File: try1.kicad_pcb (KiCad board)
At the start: 2 copper layers, 168.9 x 102 mm, 33 parts, among them J10 Archon-connector-modules-Driv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, J11 Archon-connector-modules-Driv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, J2 Archon-connector-modules-Heat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, J21 DB37, J22 DB37, J3 Archon-connector-modules-Driv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, J31 DB9, J4 Archon-connector-modules-LVBi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, J41 CONN_DVI, J5 Archon-connector-modules-ADC, J6 Archon-connector-modules-ADC, J7 Archon-connector-modules-ADC, J8 Archon-connector-modules-ADC, J9 Archon-connector-modules-HVBi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, P1 CONN_02X02

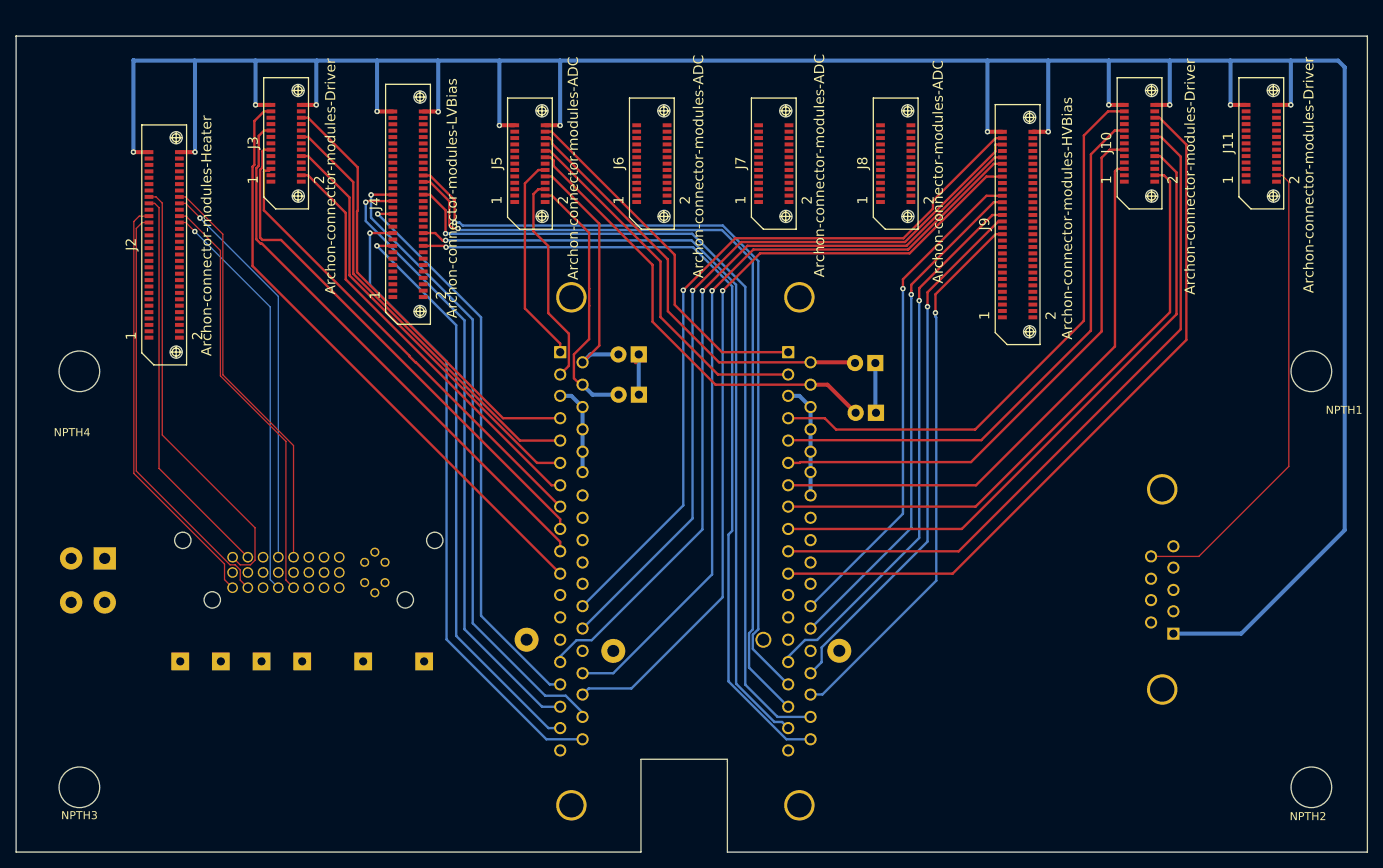
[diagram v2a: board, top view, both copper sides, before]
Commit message: WIP Add Last Driver Traces
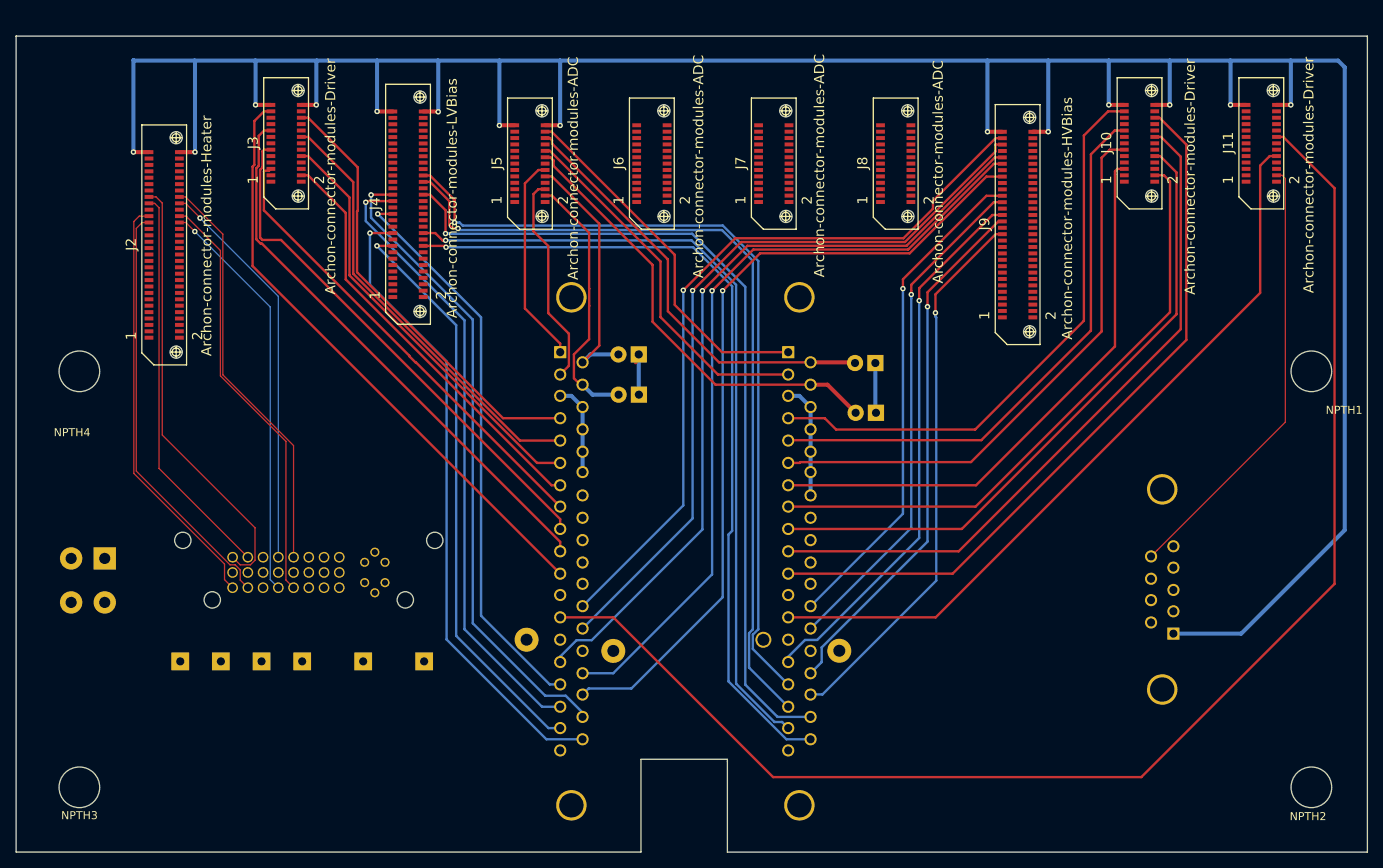
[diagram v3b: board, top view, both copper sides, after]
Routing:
- net /~ResetLog_L: track 0.41 -> 174.9 mm
- net /~ResetLog_R: track 0.00 -> 94.2 mm
- net FLASH_V: track 59.3 -> 55.5 mm
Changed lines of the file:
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@@
     (thickness 1.6)
     (drawings 37)
-    (tracks 527)
+    (tracks 539)
     (zones 0)
     (modules 33)
@@
   (segment (start 192.37 36.66) (end 192.37 61.08) (width 0.3) (layer F.Cu) (net 319))
   (segment (start 189.01214 33.30214) (end 192.37 36.66) (width 0.3) (layer F.Cu) (net 319))
+  (segment (start 203.63992 38.09766) (end 202.79001 38.09766) (width 0.3) (layer F.Cu) (net 320))
+  (segment (start 161.042 95.755) (end 142.603 95.755) (width 0.3) (layer F.Cu) (net 320))
+  (segment (start 202.79001 38.09766) (end 201.5982 39.28947) (width 0.3) (layer F.Cu) (net 320))
+  (segment (start 201.5982 39.28947) (end 201.5982 55.1988) (width 0.3) (layer F.Cu) (net 320))
+  (segment (start 201.5982 55.1988) (end 161.042 95.755) (width 0.3) (layer F.Cu) (net 320))
+  (segment (start 203.63992 35.70244) (end 204.48983 35.70244) (width 0.3) (layer F.Cu) (net 321))
+  (segment (start 140.7144 115.727) (end 120.7424 95.755) (width 0.3) (layer F.Cu) (net 321))
+  (segment (start 120.7424 95.755) (end 114.103 95.755) (width 0.3) (layer F.Cu) (net 321))
+  (segment (start 204.48983 35.70244) (end 210.8946 42.10721) (width 0.3) (layer F.Cu) (net 321))
+  (segment (start 210.8946 42.10721) (end 210.8946 91.5716) (width 0.3) (layer F.Cu) (net 321))
+  (segment (start 210.8946 91.5716) (end 186.7392 115.727) (width 0.3) (layer F.Cu) (net 321))
+  (segment (start 186.7392 115.727) (end 140.7144 115.727) (width 0.3) (layer F.Cu) (net 321))
   (segment (start 203.63992 35.70244) (end 204.050132 35.70244) (width 0.1524) (layer F.Cu) (net 321) (status 30))
-  (segment (start 203.63992 40.49796) (end 204.34223 40.49796) (width 0.1524) (layer F.Cu) (net 322) (status 10))
-  (segment (start 204.34223 40.49796) (end 205.1812 41.33693) (width 0.1524) (layer F.Cu) (net 322))
-  (segment (start 205.1812 41.33693) (end 205.1812 76.8858) (width 0.1524) (layer F.Cu) (net 322))
-  (segment (start 205.1812 76.8858) (end 193.929 88.138) (width 0.1524) (layer F.Cu) (net 322))
-  (segment (start 193.929 88.138) (end 187.96 88.138) (width 0.1524) (layer F.Cu) (net 322) (status 20))
+  (segment (start 188.721999 87.376001) (end 187.96 88.138) (width 0.1524) (layer F.Cu) (net 322))
+  (segment (start 204.743788 71.354212) (end 188.721999 87.376001) (width 0.1524) (layer F.Cu) (net 322))
+  (segment (start 204.743788 40.899518) (end 204.743788 71.354212) (width 0.1524) (layer F.Cu) (net 322))
+  (segment (start 204.34223 40.49796) (end 204.743788 40.899518) (width 0.1524) (layer F.Cu) (net 322))
+  (segment (start 203.63992 40.49796) (end 204.34223 40.49796) (width 0.1524) (layer F.Cu) (net 322))
   (segment (start 135.6 54.369388) (end 130.722228 49.491616) (width 0.3) (layer B.Cu) (net 343))
   (segment (start 130.722228 49.491616) (end 99.829114 49.491616) (width 0.3) (layer B.Cu) (net 343))

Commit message: Finish Main Rerouting After Edge, High Current Fixes
This is a milestone.  After updating the size/edge of the board
and correcting the erroneous connections that were supposed to be
high current biases, I have *roughly* placed most of the traces.
I still need to finish the Heater traces and adjust all of the traces
for ideal spacing.

First, however, I'm going to expose GPIO pins; then I'll make the final
passes on the routes.
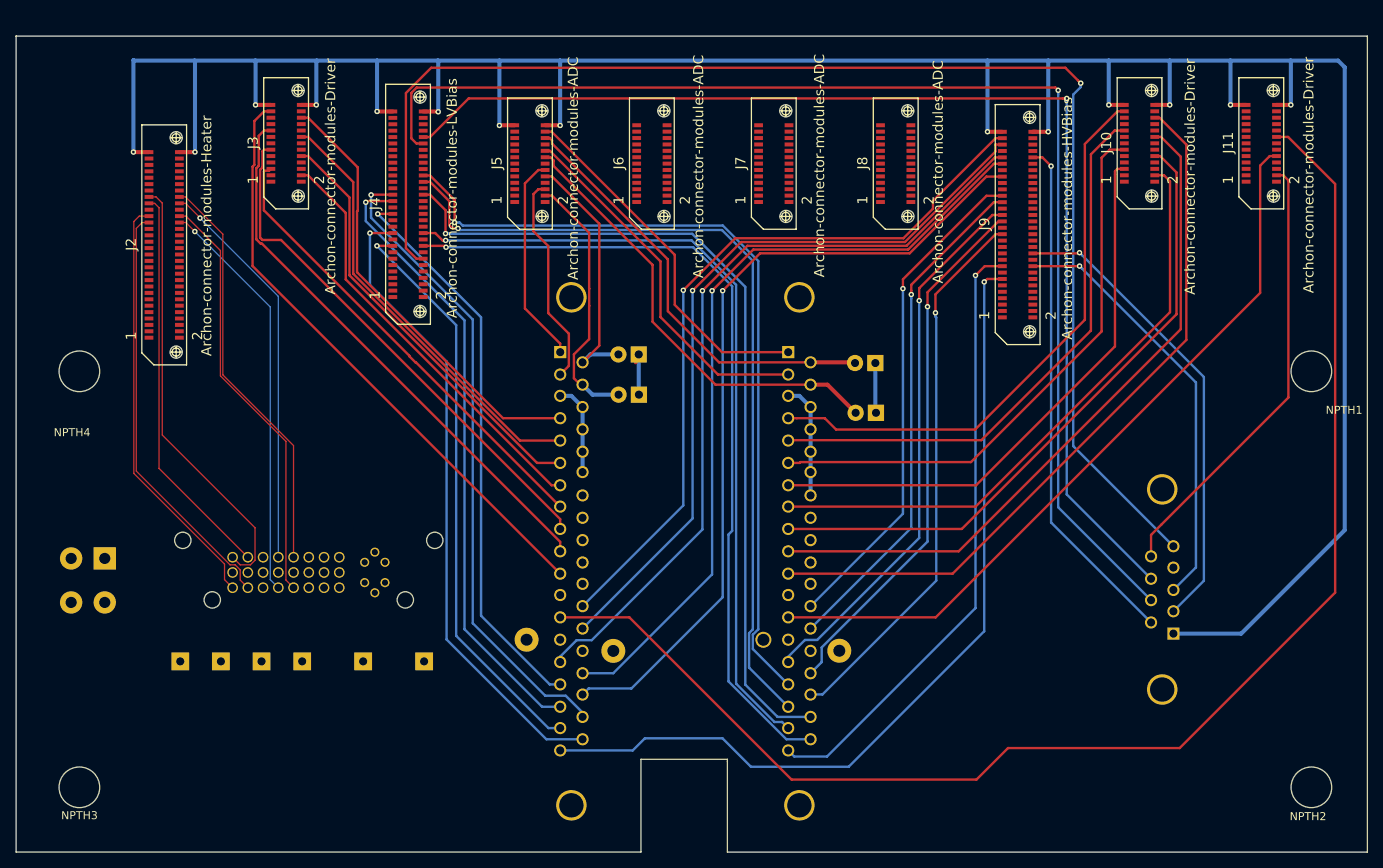
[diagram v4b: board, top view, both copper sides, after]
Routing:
- net LED_+15V: track 0.00 -> 172.0 mm, vias 0 -> 1
- net SEL_LED_1: track 0.00 -> 157.2 mm, vias 0 -> 1
- net SEL_LED_2: track 0.00 -> 146.8 mm, vias 0 -> 1
- net /+5V_L: track 0.00 -> 108.2 mm, vias 0 -> 1
- net /+5V_R: track 0.00 -> 76.8 mm, vias 0 -> 1
- net SHUT_OUT: track 0.00 -> 65.0 mm, vias 0 -> 1
- net LED_PWR: track 0.00 -> 58.7 mm, vias 0 -> 1
- net LED_+5: track 0.00 -> 53.5 mm, vias 0 -> 1
- net /~ResetLog_L: track 174.9 -> 176.2 mm
- net /S3X: track 72.6 -> 72.0 mm

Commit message: Expose GPIO Pins
I'm not sure this is exactly what we want, but the core is done.  If we
want to change the footprint for these pins or move them, it will be
relatively easy, now that the connections have been made.
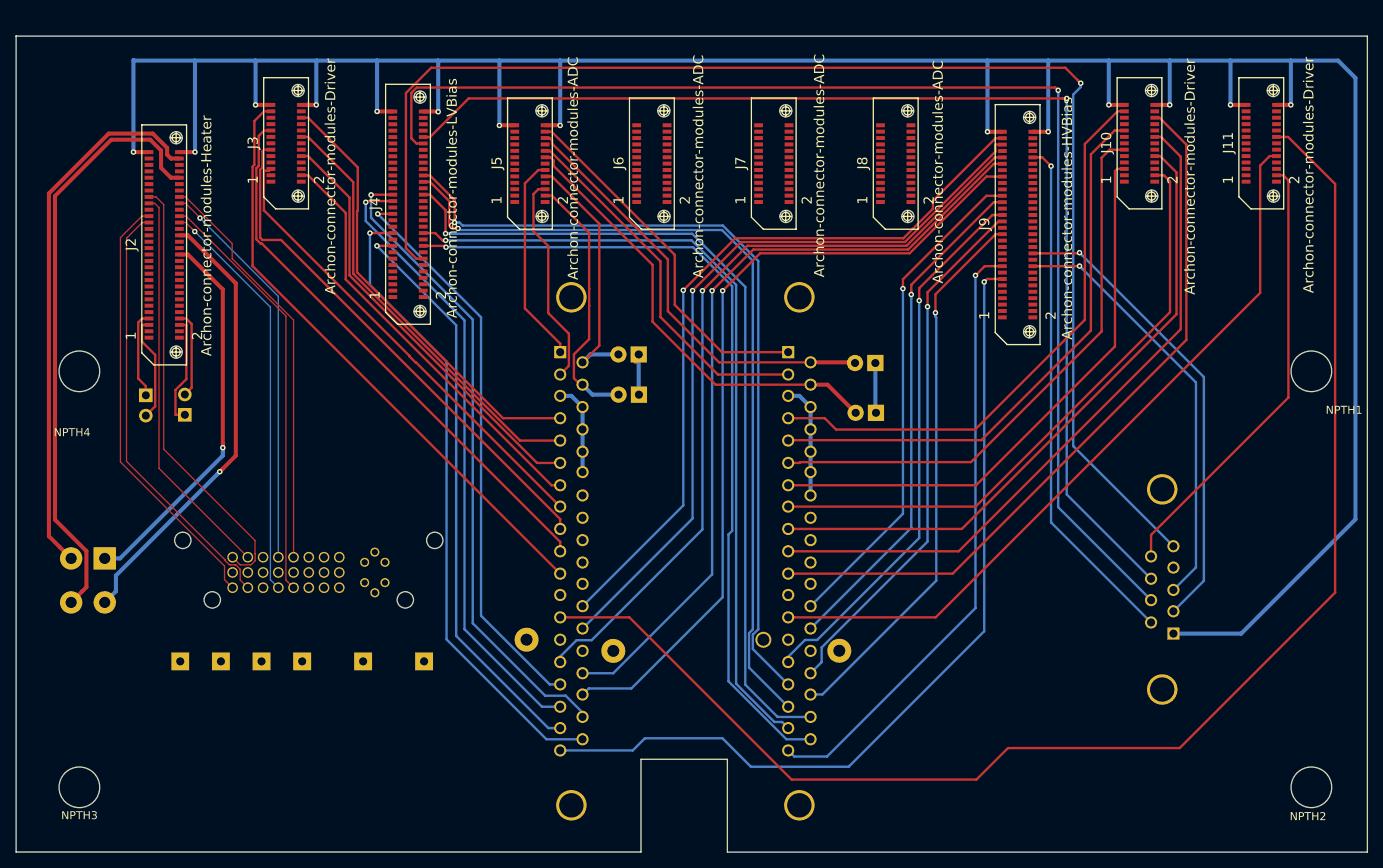
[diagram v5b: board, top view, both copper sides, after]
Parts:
- added J51: Conn_01x02_Male, Pin_Headers:Pin_Header_Straight_1x02_Pitch2.54mm, B.Cu at (62.3, 68.0)
- added J52: Conn_01x02_Male, Pin_Headers:Pin_Header_Straight_1x02_Pitch2.54mm, B.Cu at (67.2, 70.4)
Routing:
- net HEATER1_BN: track 0.00 -> 74.9 mm
- net HEATER1_BP: track 0.00 -> 68.0 mm
- net HEATER1_AN: track 0.00 -> 56.2 mm, vias 0 -> 1
- net HEATER1_AP: track 0.00 -> 48.1 mm, vias 0 -> 1
- net Net-(J2-Pad6): track 0.00 -> 13.8 mm
- net Net-(J2-Pad5): track 0.00 -> 13.4 mm
- net Net-(J2-Pad7): track 0.00 -> 11.0 mm
- net Net-(J2-Pad8): track 0.00 -> 11.0 mm
- net HEATER1_TEMPA_FN: track 53.1 -> 54.3 mm
- net /GND: track 403.8 -> 405.0 mm
- net HEATER1_TEMPA_FP: track 53.0 -> 54.1 mm

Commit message: Some Fine Tuning
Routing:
- net /TGY: track 58.7 -> 61.6 mm
- net /VLg_R: track 103.0 -> 100.4 mm
- net /P2Y: track 70.1 -> 72.3 mm
- net /P1Y: track 75.2 -> 77.3 mm
- net /SWY: track 53.3 -> 55.3 mm
- net /S1Y: track 54.0 -> 55.5 mm
- net /ResetLO_R: track 106.3 -> 107.5 mm
- net /S2Y: track 54.8 -> 55.8 mm
- net /P3Y: track 65.4 -> 66.3 mm
- net /GainSW2_R: track 105.0 -> 104.1 mm
- net /-15V_R: track 103.6 -> 103.0 mm

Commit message: More Fine Tuning
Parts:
- moved W3 2.24 mm to (150.0, 97.9)
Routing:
- net DVI_P9_SPARET5: track 0.00 -> 18.4 mm
- net DVI_P9_SPARET6: track 0.00 -> 15.0 mm
- net DVI_P9_SPARET1: track 0.00 -> 14.6 mm
- net DVI_P9_SPARET2: track 0.00 -> 13.3 mm
- net DVI_P9_SPARET3: track 0.00 -> 12.7 mm
- net DVI_P9_SPARET4: track 0.00 -> 11.6 mm
- net /Spare_2: track 0.00 -> 5.43 mm
- net /Spare_3: track 0.00 -> 4.20 mm
- net /Spare_4: track 0.00 -> 3.84 mm
- net /Spare_1: track 0.00 -> 3.11 mm
- net /ResetLO_R: track 107.5 -> 105.2 mm
- net /GainSW2_R: track 104.1 -> 102.0 mm
- net /VDD_C: track 66.7 -> 68.3 mm
- net /TGX: track 91.6 -> 92.9 mm
- net /P3X: track 86.8 -> 87.8 mm
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
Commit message: More Fine Tuning
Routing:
- net /+5V_L: track 108.2 -> 105.9 mm
- net /ResetLO_R: track 105.2 -> 103.0 mm
- net /+15V_R: track 100.8 -> 98.8 mm
- net /GainSW2_R: track 102.0 -> 100.1 mm
- net /VLg_R: track 100.4 -> 98.7 mm
- net SEL_LED_1: track 157.2 -> 158.7 mm
- net /-15V_R: track 102.6 -> 101.2 mm
- net SEL_LED_2: track 146.8 -> 148.1 mm
- net /+5V_R: track 76.8 -> 75.7 mm
- net LED_+15V: track 172.0 -> 170.9 mm
- net /~ResetLog_L: track 176.2 -> 175.2 mm
